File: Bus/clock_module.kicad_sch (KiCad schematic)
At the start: 1 part, among them J1 Conn_01x05_Pin

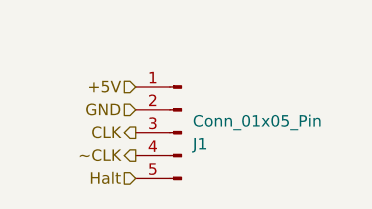
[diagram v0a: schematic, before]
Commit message: Some initial bus layout
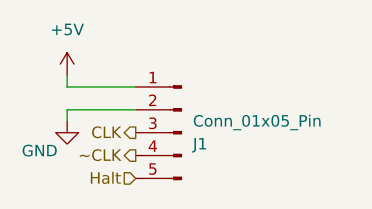
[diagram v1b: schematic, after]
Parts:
- J1: footprint (none) -> Connector_PinHeader_2.54mm:PinHeader_1x05_P2.54mm_Vertical
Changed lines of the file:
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@@
 	(generator_version "8.0")
 	(paper "A4")
-	(hierarchical_label "+5V"
-		(shape input)
-		(at 248.92 38.1 180)
+	(wire
+		(pts
+			(xy 241.3 40.64) (xy 248.92 40.64)
+		)
+		(stroke
+			(width 0)
+			(type default)
+		)
+	)
+	(wire
+		(pts
+			(xy 241.3 38.1) (xy 241.3 36.83)
+		)
+		(stroke
+			(width 0)
+			(type default)
+		)
+	)
+	(wire
+		(pts
+			(xy 241.3 41.91) (xy 241.3 40.64)
+		)
+		(stroke
+			(width 0)
+			(type default)
+		)
+	)
+	(wire
+		(pts
+			(xy 248.92 38.1) (xy 241.3 38.1)
+		)
+		(stroke
+			(width 0)
+			(type default)
+		)
+	)
+	(hierarchical_label "~CLK"
+		(shape output)
+		(at 248.92 45.72 180)
 		(fields_autoplaced yes)
 		(effects
@@
 		)
 	)
-	(hierarchical_label "GND"
-		(shape input)
-		(at 248.92 40.64 180)
+	(hierarchical_label "CLK"
+		(shape output)
+		(at 248.92 43.18 180)
 		(fields_autoplaced yes)
 		(effects
@@
 		)
 	)
-	(hierarchical_label "~CLK"
-		(shape output)
-		(at 248.92 45.72 180)
+	(hierarchical_label "Halt"
+		(shape input)
+		(at 248.92 48.26 180)
 		(fields_autoplaced yes)
 		(effects
@@
 		)
 	)
-	(hierarchical_label "CLK"
-		(shape output)
-		(at 248.92 43.18 180)
-		(fields_autoplaced yes)
-		(effects
-			(font
-				(size 1.27 1.27)
-			)
-			(justify right)
-		)
-	)
-	(hierarchical_label "Halt"
-		(shape input)
-		(at 248.92 48.26 180)
-		(fields_autoplaced yes)
-		(effects
-			(font
-				(size 1.27 1.27)
-			)
-			(justify right)
+	(symbol
+		(lib_id "power:GND")
+		(at 241.3 41.91 0)
+		(unit 1)
+		(exclude_from_sim no)
+		(in_bom yes)
+		(on_board yes)
+		(dnp no)
+		(property "Reference" "#PWR06"
+			(at 241.3 48.26 0)
+			(effects
+				(font
+					(size 1.27 1.27)
+				)
+				(hide yes)
+			)
+		)
+		(property "Value" "GND"
+			(at 238.252 45.212 0)
+			(effects
+				(font
+					(size 1.27 1.27)
+				)
+			)
+		)
+		(property "Footprint" ""
+			(at 241.3 41.91 0)
+			(effects
+				(font
+					(size 1.27 1.27)
+				)
+				(hide yes)
+			)
+		)
+		(property "Datasheet" ""
+			(at 241.3 41.91 0)
+			(effects
+				(font
+					(size 1.27 1.27)
+				)
+				(hide yes)
+			)
+		)
+		(property "Description" "Power symbol creates a global label with name \"GND\" , ground"
+			(at 241.3 41.91 0)
+			(effects
+				(font
+					(size 1.27 1.27)
+				)
+				(hide yes)
+			)
+		)
+		(pin "1"
+		)
+		(instances
+			(project "bus"
+				(path "/37ae8b13-e183-404e-b70a-681e1af60f55/47d3b732-6cda-4ad5-90e6-a3d17299e2c5"
+					(reference "#PWR06")
+					(unit 1)
+				)
+			)
 		)
 	)
@@
 			)
 		)
-		(property "Footprint" ""
+		(property "Footprint" "Connector_PinHeader_2.54mm:PinHeader_1x05_P2.54mm_Vertical"
 			(at 254 43.18 0)
 			(effects
@@
 					(unit 1)
 				)
+			)
+		)
+	)
+	(symbol
+		(lib_id "power:+5V")
+		(at 241.3 36.83 0)
+		(unit 1)
+		(exclude_from_sim no)
+		(in_bom yes)
+		(on_board yes)
+		(dnp no)
+		(fields_autoplaced yes)
+		(property "Reference" "#PWR05"
+			(at 241.3 40.64 0)
+			(effects
+				(font
+					(size 1.27 1.27)
+				)
+				(hide yes)
+			)
+		)
+		(property "Value" "+5V"
+			(at 241.3 31.75 0)
+			(effects
+				(font
+					(size 1.27 1.27)
+				)
+			)
+		)
+		(property "Footprint" ""
+			(at 241.3 36.83 0)
+			(effects
+				(font
+					(size 1.27 1.27)
+				)
+				(hide yes)
+			)
+		)
+		(property "Datasheet" ""
+			(at 241.3 36.83 0)
+			(effects
+				(font
+					(size 1.27 1.27)
+				)
+				(hide yes)
+			)
+		)
+		(property "Description" "Power symbol creates a global label with name \"+5V\""
+			(at 241.3 36.83 0)
+			(effects
+				(font
+					(size 1.27 1.27)
+				)
+				(hide yes)
+			)
+		)
+		(pin "1"
+		)
+		(instances
+			(project "bus"
+				(path "/37ae8b13-e183-404e-b70a-681e1af60f55/47d3b732-6cda-4ad5-90e6-a3d17299e2c5"
+					(reference "#PWR05")
+					(unit 1)
+				)

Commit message: Updated bus schematics with pinout of MAR/ALU/Registers on PCBs ordered
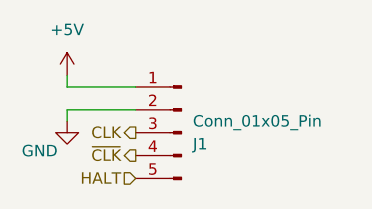
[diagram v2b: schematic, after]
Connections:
- net Halt renamed HALT
- net ~CLK renamed ~{CLK}
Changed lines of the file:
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@@
 		)
 	)
-	(hierarchical_label "~CLK"
+	(hierarchical_label "~{CLK}"
 		(shape output)
 		(at 248.92 45.72 180)
@@
 		)
 	)
-	(hierarchical_label "Halt"
+	(hierarchical_label "HALT"
 		(shape input)
 		(at 248.92 48.26 180)
